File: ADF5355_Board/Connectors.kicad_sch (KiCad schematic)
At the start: 5 parts, among them J1 Conn_01x02, J2 USB_B_Micro, J3 Conn_Coaxial, J4 Conn_Coaxial, J5 Conn_Coaxial

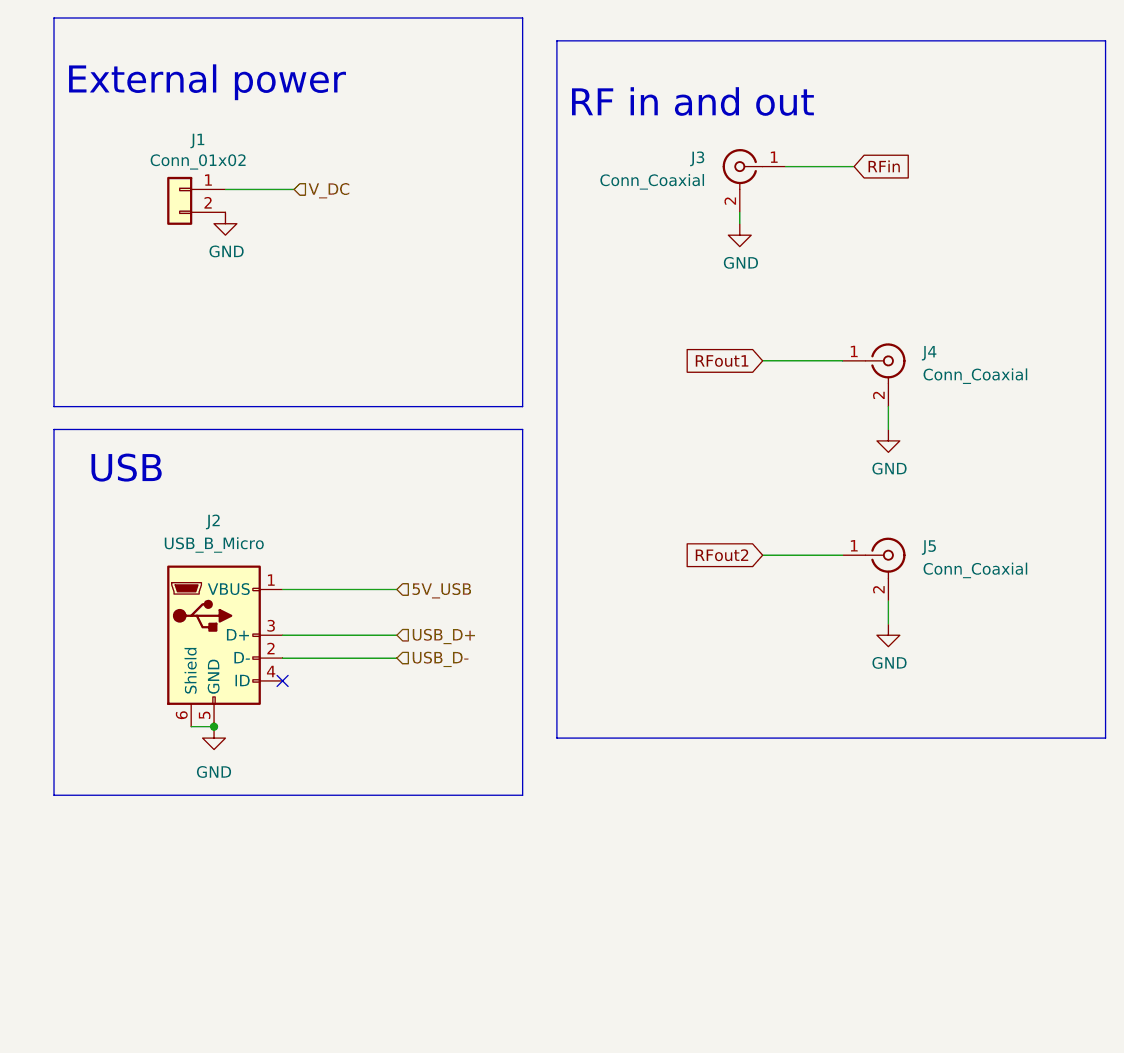
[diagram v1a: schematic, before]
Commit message: Finished MCU board
Finished MCU board and started finishing up the VCO board
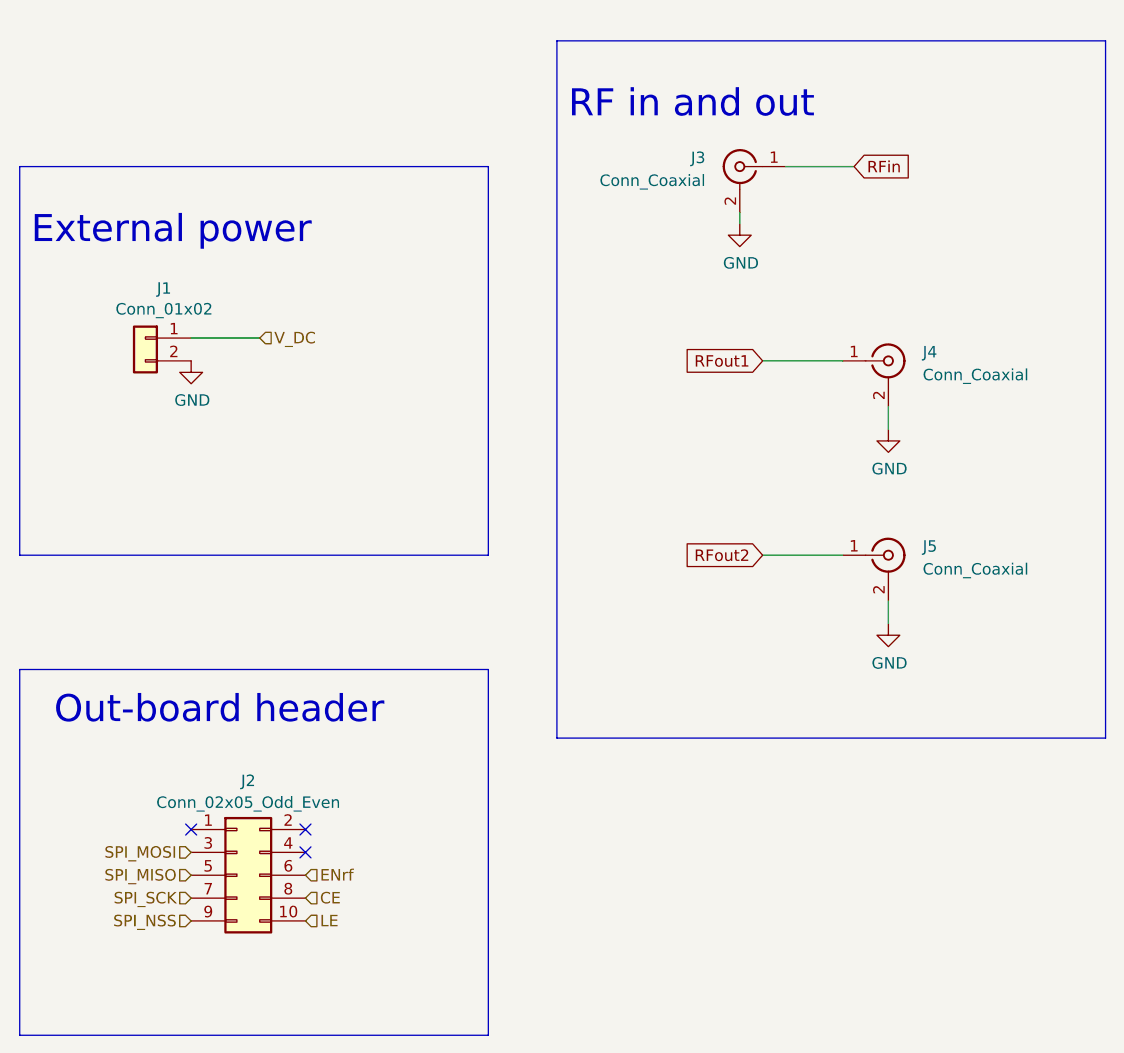
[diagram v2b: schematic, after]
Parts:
- removed J2: USB_B_Micro, Connector_USB:USB_Micro-B_Amphenol_10118194_Horizontal, symbol Connector:USB_B_Micro
- added J2: Conn_02x05_Odd_Even, Connector_PinHeader_2.54mm:PinHeader_2x05_P2.54mm_Vertical, symbol Connector_Generic:Conn_02x05_Odd_Even
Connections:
- new net CE: J2.8 (Pin_8)
- new net ENrf: J2.6 (Pin_6)
- new net LE: J2.10 (Pin_10)
- new net SPI_MISO: J2.5 (Pin_5)
- new net SPI_MOSI: J2.3 (Pin_3)
- new net SPI_NSS: J2.9 (Pin_9)
- new net SPI_SCK: J2.7 (Pin_7)
- no-connect marks 1 -> 3
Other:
- note added: "Out-board header"
- note removed: "USB"
- moved on the sheet: J1

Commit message: IDK where I stopped
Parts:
- removed J1: Conn_01x02, Connector:Banana_Cliff_FCR7350x_S16N-PC_Horizontal, symbol Connector_Generic:Conn_01x02
- added J1, J7: Conn_01x01, ADF5355:deltron-571-0500-4mm-90deg-single-socket, symbol Connector_Generic:Conn_01x01
- added J6: Conn_Coaxial, Connector_Coaxial:SMA_Molex_73251-1153_EdgeMount_Horizontal, symbol Connector:Conn_Coaxial
- added J8: Conn_01x02, ADF5355:d2269_100-1512192, symbol Connector_Generic:Conn_01x02
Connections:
- net GND: now also J6.2 (Ext), J7.1 (Pin_1), J8.2 (Pin_2)
- net V_DC: now also J1.1 (Pin_1), J8.1 (Pin_1)
- net MUXout: now reaches J2.4 (Pin_4)
- net SPI_MISO: no longer names the net of J2.5 (Pin_5)
- net SPI_NSS: no longer names the net of J2.9 (Pin_9)
- new net RFout3: J6.1 (In)
- no-connect marks 3 -> 2
